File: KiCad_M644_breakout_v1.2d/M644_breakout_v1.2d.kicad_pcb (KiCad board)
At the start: 2 copper layers, 54.9 x 45 mm, 64 parts, among them IC1 ATMEGA16/32/644/1284, IC2 78TV, Q1 16Mhz, SW1/PC5 SMD_TACT_4x4, X2 DG300-5.0-02P-12

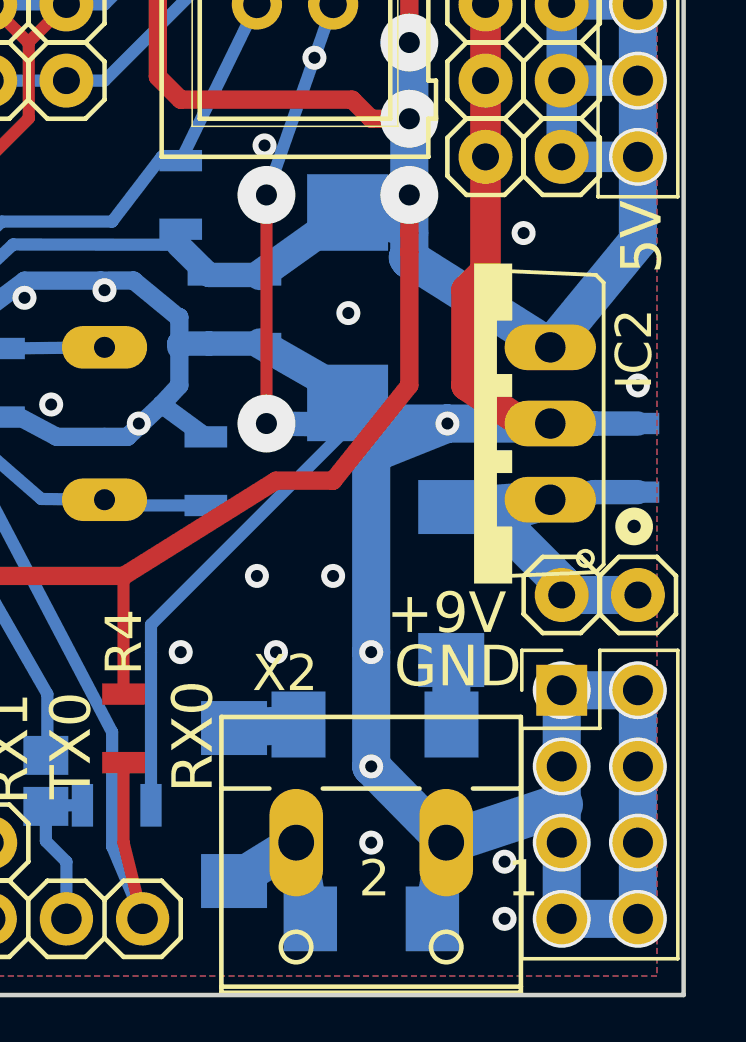
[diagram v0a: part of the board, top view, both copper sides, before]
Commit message: Remove 3 diodes
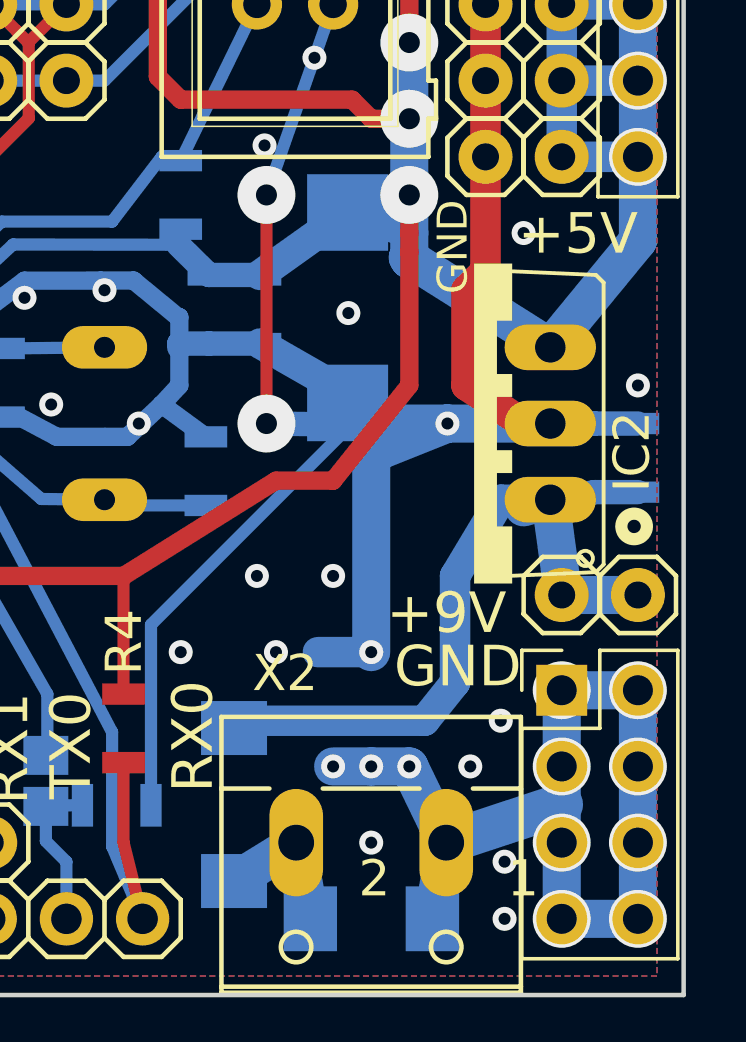
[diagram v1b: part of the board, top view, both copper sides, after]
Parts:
- removed D2, D4: SM4007, M644_breakout_v1.2d:DO214AA
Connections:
- D1 pad C: Net-(D1-PadC) -> Net-(C4-PadP$1)
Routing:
- net Net-(C4-PadP$1): track 14.7 -> 26.8 mm
- net GND: track 247.6 -> 250.0 mm, vias 55 -> 59
- net Net-(D1-PadC): track 2.15 -> 0.00 mm
- net Net-(D2-PadC): track 2.15 -> 0.00 mm
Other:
- board text removed: "5V"
